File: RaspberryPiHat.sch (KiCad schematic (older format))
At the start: 7 parts, among them J1 Raspberry_Pi_2_3, SW1 SW_DPST, U1 DHT22

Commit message: Finished Schematic
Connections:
- net at J1.1 (3V3): now also R2.2, SW1.1, SW1.3, U1.1 (VCC)
- net at J1.11 (GPIO17): now also R2.1, U1.2 (IO)
- net at J1.6 (GND): now also R1.2, U1.4 (GND)
- net at J1.7 (GCLK0/GPIO4): now also R3.1
- net at J1.8 (GPIO14/TXD): now also R1.1, SW1.2, SW1.4
- net at J1.9 (GND): now also D1.1 (K)
- net at R3.2: now also D1.2 (A)
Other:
- moved on the sheet: D1, R1, R2, R3, SW1, U1
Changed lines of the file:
@@
 L Switch:SW_DPST SW1
 U 1 1 5CDA4549
-P 3200 3025
-F 0 "SW1" H 3200 3350 50  0000 C CNN
-F 1 "SW_DPST" H 3200 3259 50  0000 C CNN
-F 2 "freetronics_footprints:SW_PUSHBUTTON_PTH" H 3200 3025 50  0001 C CNN
-F 3 "~" H 3200 3025 50  0001 C CNN
-	1    3200 3025
+P 3475 2950
+F 0 "SW1" H 3475 3275 50  0000 C CNN
+F 1 "SW_DPST" H 3475 3184 50  0000 C CNN
+F 2 "freetronics_footprints:SW_PUSHBUTTON_PTH" H 3475 2950 50  0001 C CNN
+F 3 "~" H 3475 2950 50  0001 C CNN
+	1    3475 2950
 	1    0    0    -1
 $EndComp
@@
 L Device:R R3
 U 1 1 5CDA6C22
-P 6875 3650
-F 0 "R3" H 6945 3696 50  0000 L CNN
-F 1 "R" H 6945 3605 50  0000 L CNN
-F 2 "Resistor_SMD:R_0805_2012Metric" V 6805 3650 50  0001 C CNN
-F 3 "~" H 6875 3650 50  0001 C CNN
-	1    6875 3650
+P 7150 3725
+F 0 "R3" H 7220 3771 50  0000 L CNN
+F 1 "R" H 7220 3680 50  0000 L CNN
+F 2 "Resistor_SMD:R_0805_2012Metric" V 7080 3725 50  0001 C CNN
+F 3 "~" H 7150 3725 50  0001 C CNN
+	1    7150 3725
 	1    0    0    -1
 $EndComp
@@
 L Device:R R2
 U 1 1 5CDA7C16
-P 4175 2750
-F 0 "R2" H 4245 2796 50  0000 L CNN
-F 1 "R" H 4245 2705 50  0000 L CNN
-F 2 "Resistor_SMD:R_0805_2012Metric" V 4105 2750 50  0001 C CNN
-F 3 "~" H 4175 2750 50  0001 C CNN
-	1    4175 2750
-	1    0    0    -1
+P 4400 3350
+F 0 "R2" V 4193 3350 50  0000 C CNN
+F 1 "R" V 4284 3350 50  0000 C CNN
+F 2 "Resistor_SMD:R_0805_2012Metric" V 4330 3350 50  0001 C CNN
+F 3 "~" H 4400 3350 50  0001 C CNN
+	1    4400 3350
+	0    1    1    0
 $EndComp
 $Comp
 L Device:R R1
 U 1 1 5CDA8690
-P 3225 3800
-F 0 "R1" H 3295 3846 50  0000 L CNN
-F 1 "R" H 3295 3755 50  0000 L CNN
-F 2 "Resistor_SMD:R_0805_2012Metric" V 3155 3800 50  0001 C CNN
-F 3 "~" H 3225 3800 50  0001 C CNN
-	1    3225 3800
+P 3825 3275
+F 0 "R1" H 3895 3321 50  0000 L CNN
+F 1 "R" H 3895 3230 50  0000 L CNN
+F 2 "Resistor_SMD:R_0805_2012Metric" V 3755 3275 50  0001 C CNN
+F 3 "~" H 3825 3275 50  0001 C CNN
+	1    3825 3275
 	1    0    0    -1
 $EndComp
@@
 L Device:LED D1
 U 1 1 5CDA93D6
-P 6875 4100
-F 0 "D1" V 6914 3983 50  0000 R CNN
-F 1 "LED" V 6823 3983 50  0000 R CNN
-F 2 "LED_SMD:LED_0805_2012Metric" H 6875 4100 50  0001 C CNN
-F 3 "~" H 6875 4100 50  0001 C CNN
-	1    6875 4100
+P 7150 4125
+F 0 "D1" V 7189 4008 50  0000 R CNN
+F 1 "LED" V 7098 4008 50  0000 R CNN
+F 2 "LED_SMD:LED_0805_2012Metric" H 7150 4125 50  0001 C CNN
+F 3 "~" H 7150 4125 50  0001 C CNN
+	1    7150 4125
 	0    -1   -1   0
 $EndComp
@@
 L Sensor:DHT11 U1
 U 1 1 5CDAA42C
-P 3975 3350
-F 0 "U1" H 3731 3396 50  0000 R CNN
-F 1 "DHT22" H 3731 3305 50  0000 R CNN
-F 2 "Connector_PinHeader_2.54mm:PinHeader_1x03_P2.54mm_Vertical" H 3975 2950 50  0001 C CNN
-F 3 "http://akizukidenshi.com/download/ds/aosong/DHT11.pdf" H 4125 3600 50  0001 C CNN
-	1    3975 3350
+P 4075 4150
+F 0 "U1" H 3831 4196 50  0000 R CNN
+F 1 "DHT22" H 3831 4105 50  0000 R CNN
+F 2 "Connector_PinHeader_2.54mm:PinHeader_1x03_P2.54mm_Vertical" H 4075 3750 50  0001 C CNN
+F 3 "http://akizukidenshi.com/download/ds/aosong/DHT11.pdf" H 4225 4400 50  0001 C CNN
+	1    4075 4150
 	1    0    0    -1
 $EndComp
+Wire Wire Line
+	7150 4275 7150 5300
+Wire Wire Line
+	7150 5300 5400 5300
+Wire Wire Line
+	5400 5300 5400 5150
+Wire Wire Line
+	7150 3875 7150 3975
+Wire Wire Line
+	7150 3575 7150 3550
+Wire Wire Line
+	7150 3550 6500 3550
+Wire Wire Line
+	5800 2550 5800 2075
+Wire Wire Line
+	5800 2075 4075 2075
+Wire Wire Line
+	4075 2075 4075 3350
+Wire Wire Line
+	4375 4150 4725 4150
+Wire Wire Line
+	4725 4150 4725 3350
+Wire Wire Line
+	4725 3350 4900 3350
+Wire Wire Line
+	4550 3350 4725 3350
+Connection ~ 4725 3350
+Wire Wire Line
+	4250 3350 4075 3350
+Connection ~ 4075 3350
+Wire Wire Line
+	4075 3350 4075 3850
+Wire Wire Line
+	4075 4450 4075 5300
+Wire Wire Line
+	4075 5300 5300 5300
+Wire Wire Line
+	5300 5300 5300 5150
+Wire Wire Line
+	4900 2950 3825 2950
+Wire Wire Line
+	3675 2850 3675 2950
+Connection ~ 3675 2950
+Wire Wire Line
+	3675 2950 3675 3050
+Wire Wire Line
+	3825 3125 3825 2950
+Connection ~ 3825 2950
+Wire Wire Line
+	3825 2950 3675 2950
+Wire Wire Line
+	3825 3425 3825 5300
+Wire Wire Line
+	3825 5300 4075 5300
+Connection ~ 4075 5300
+Wire Wire Line
+	3275 2850 3275 2950
+Wire Wire Line
+	3275 2950 2825 2950
+Wire Wire Line
+	2825 2950 2825 2075
+Wire Wire Line
+	2825 2075 4075 2075
+Connection ~ 3275 2950
+Wire Wire Line
+	3275 2950 3275 3050
+Connection ~ 4075 2075
 $EndSCHEMATC

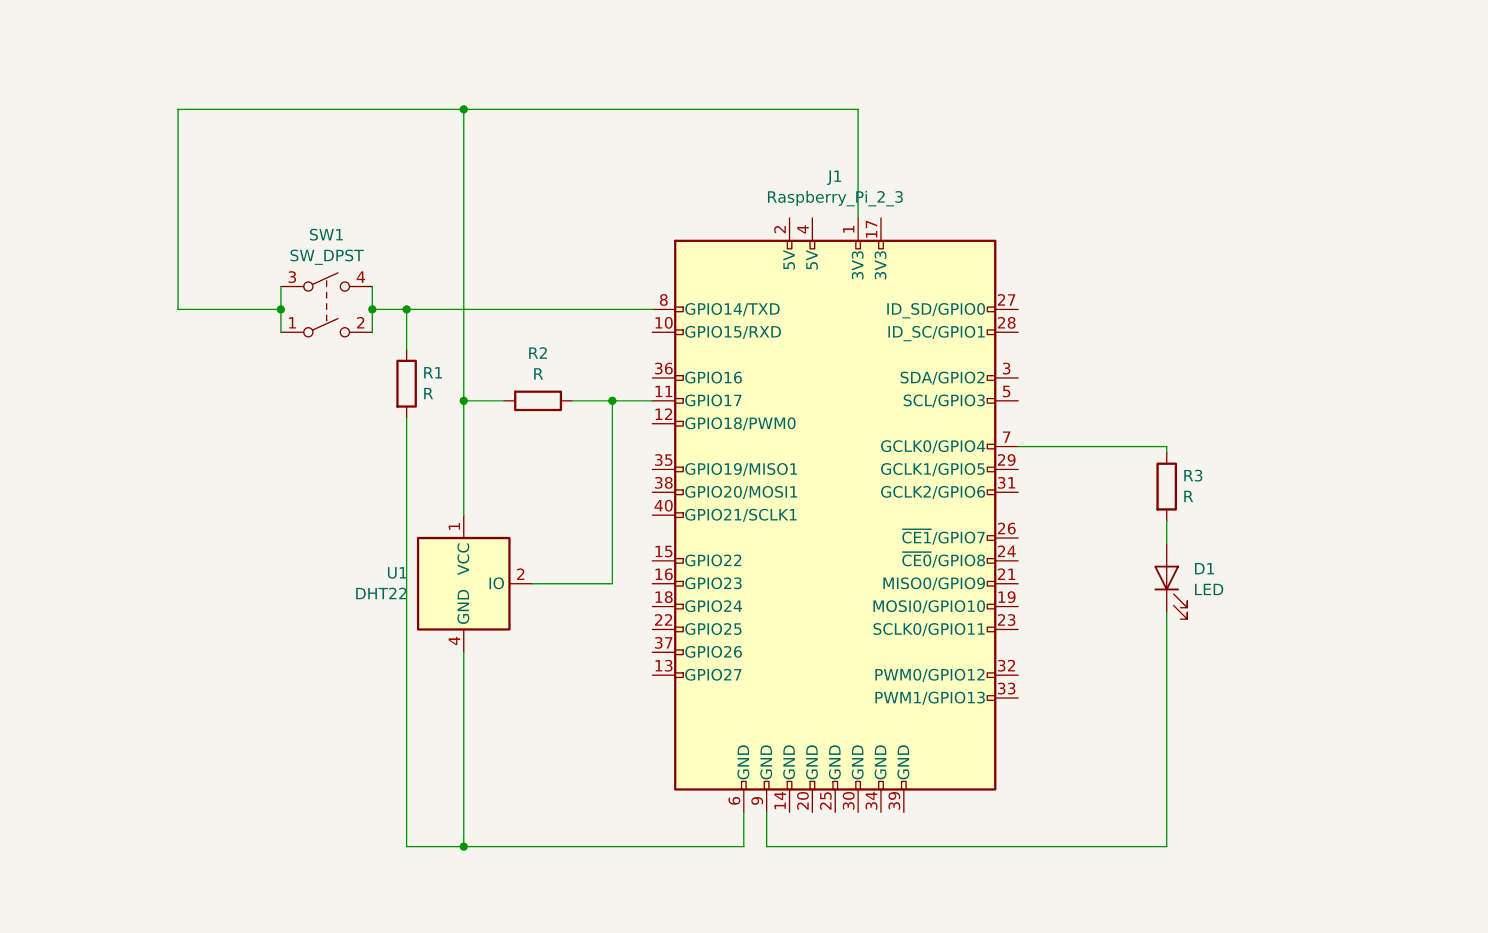
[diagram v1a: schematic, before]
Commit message: Passed DRC
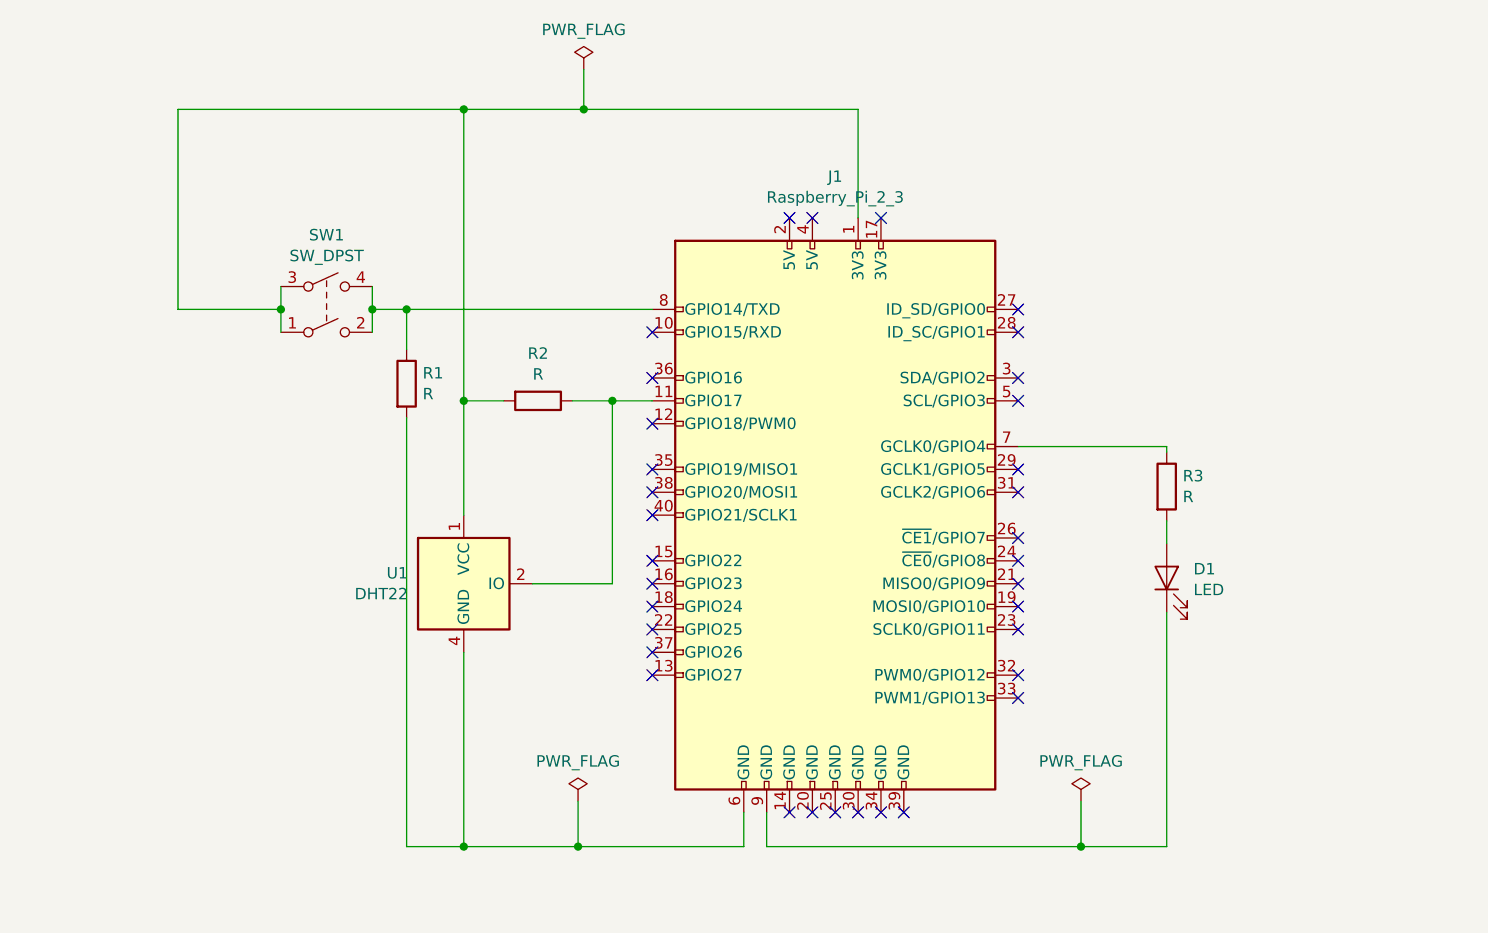
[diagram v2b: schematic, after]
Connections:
- no-connect marks 0 -> 34
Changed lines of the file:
@@
 	7150 4275 7150 5300
 Wire Wire Line
-	7150 5300 5400 5300
+	7150 5300 6775 5300
 Wire Wire Line
 	5400 5300 5400 5150
@@
 	5800 2550 5800 2075
 Wire Wire Line
-	5800 2075 4075 2075
+	5800 2075 4600 2075
 Wire Wire Line
 	4075 2075 4075 3350
@@
 	4075 4450 4075 5300
 Wire Wire Line
-	4075 5300 5300 5300
+	4075 5300 4575 5300
 Wire Wire Line
 	5300 5300 5300 5150
@@
 	3275 2950 3275 3050
 Connection ~ 4075 2075
+NoConn ~ 4900 3050
+NoConn ~ 4900 3250
+NoConn ~ 4900 3450
+NoConn ~ 4900 3650
+NoConn ~ 4900 3750
+NoConn ~ 4900 3850
+NoConn ~ 4900 4050
+NoConn ~ 4900 4150
+NoConn ~ 4900 4250
+NoConn ~ 4900 4350
+NoConn ~ 4900 4450
+NoConn ~ 4900 4550
+NoConn ~ 5500 5150
+NoConn ~ 5600 5150
+NoConn ~ 5700 5150
+NoConn ~ 5800 5150
+NoConn ~ 5900 5150
+NoConn ~ 6000 5150
+NoConn ~ 6500 4650
+NoConn ~ 6500 4550
+NoConn ~ 6500 4350
+NoConn ~ 6500 4250
+NoConn ~ 6500 4150
+NoConn ~ 6500 4050
+NoConn ~ 6500 3950
+NoConn ~ 6500 3750
+NoConn ~ 6500 3650
+NoConn ~ 6500 3350
+NoConn ~ 6500 3250
+NoConn ~ 6500 3050
+NoConn ~ 6500 2950
+NoConn ~ 5900 2550
+NoConn ~ 5600 2550
+NoConn ~ 5500 2550
+$Comp
+L power:PWR_FLAG #FLG0101
+U 1 1 5CDD84E3
+P 4600 1900
+F 0 "#FLG0101" H 4600 1975 50  0001 C CNN
+F 1 "PWR_FLAG" H 4600 2073 50  0000 C CNN
+F 2 "" H 4600 1900 50  0001 C CNN
+F 3 "~" H 4600 1900 50  0001 C CNN
+	1    4600 1900
+	1    0    0    -1
+$EndComp
+Wire Wire Line
+	4600 1900 4600 2075
+Connection ~ 4600 2075
+Wire Wire Line
+	4600 2075 4075 2075
+$Comp
+L power:PWR_FLAG #FLG0102
+U 1 1 5CDD996D
+P 4575 5100
+F 0 "#FLG0102" H 4575 5175 50  0001 C CNN
+F 1 "PWR_FLAG" H 4575 5273 50  0000 C CNN
+F 2 "" H 4575 5100 50  0001 C CNN
+F 3 "~" H 4575 5100 50  0001 C CNN
+	1    4575 5100
+	1    0    0    -1
+$EndComp
+$Comp
+L power:PWR_FLAG #FLG0103
+U 1 1 5CDDA483
+P 6775 5100
+F 0 "#FLG0103" H 6775 5175 50  0001 C CNN
+F 1 "PWR_FLAG" H 6775 5273 50  0000 C CNN
+F 2 "" H 6775 5100 50  0001 C CNN
+F 3 "~" H 6775 5100 50  0001 C CNN
+	1    6775 5100
+	1    0    0    -1
+$EndComp
+Wire Wire Line
+	4575 5100 4575 5300
+Connection ~ 4575 5300
+Wire Wire Line
+	4575 5300 5300 5300
+Wire Wire Line
+	6775 5100 6775 5300
+Connection ~ 6775 5300
+Wire Wire Line
+	6775 5300 5400 5300
 $EndSCHEMATC

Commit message: generated netlist
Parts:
- added D2: LED, LED_SMD:LED_0805_2012Metric, symbol Device:LED
- added R4: R, Resistor_SMD:R_0805_2012Metric, symbol Device:R
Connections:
- net 3v3: now reaches J1.1 (3V3), R2.2, SW1.1, SW1.3, U1.1 (VCC)
- net 3v3: now also R4.1
- net GND: now reaches J1.6 (GND), R1.2, U1.4 (GND)
- net GND: now also D1.1 (K), J1.9 (GND), D2.1 (K)
- net button_input: now reaches J1.8 (GPIO14/TXD), R1.1, SW1.2, SW1.4
- new net: D2.2 (A), R4.2
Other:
- note added: "N1 - Momentary Button\n"
- note added: "N2 - Sensor"
- note added: "N3 - Raspberry Pi"
- note added: "N4 - Inidcator LED"
- note added: "N5 - Power LED"
- moved on the sheet: R1, SW1

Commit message: Updated files
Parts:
- J1: footprint Connector_PinSocket_2.54mm:PinSocket_2x08_P2.54mm_Vertical -> Connector_PinHeader_2.54mm:PinHeader_2x08_P2.54mm_Vertical
- U1: footprint Connector_PinHeader_2.54mm:PinHeader_1x03_P2.54mm_Vertical -> Connector_PinHeader_2.54mm:PinHeader_1x04_P2.54mm_Vertical
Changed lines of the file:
@@
 F 0 "J1" H 6025 5350 50  0000 C CNN
 F 1 "Raspberry_Pi_2_3" H 6300 5250 50  0000 C CNN
-F 2 "Connector_PinSocket_2.54mm:PinSocket_2x08_P2.54mm_Vertical" H 5700 3850 50  0001 C CNN
+F 2 "Connector_PinHeader_2.54mm:PinHeader_2x08_P2.54mm_Vertical" H 5700 3850 50  0001 C CNN
 F 3 "https://www.raspberrypi.org/documentation/hardware/raspberrypi/schematics/rpi_SCH_3bplus_1p0_reduced.pdf" H 5700 3850 50  0001 C CNN
 	1    5700 3850
@@
 	1    7150 4125
 	0    -1   -1   0
-$EndComp
-$Comp
-L Sensor:DHT11 U1
-U 1 1 5CDAA42C
-P 4075 4150
-F 0 "U1" H 3831 4196 50  0000 R CNN
-F 1 "DHT22" H 3831 4105 50  0000 R CNN
-F 2 "Connector_PinHeader_2.54mm:PinHeader_1x03_P2.54mm_Vertical" H 4075 3750 50  0001 C CNN
-F 3 "http://akizukidenshi.com/download/ds/aosong/DHT11.pdf" H 4225 4400 50  0001 C CNN
-	1    4075 4150
-	1    0    0    -1
 $EndComp
 Wire Wire Line
@@
 Text Notes 7650 2225 0    50   ~ 0
 N5 - Power LED
+$Comp
+L Sensor:DHT11 U1
+U 1 1 5CDAA42C
+P 4075 4150
+F 0 "U1" H 3831 4196 50  0000 R CNN
+F 1 "DHT22" H 3831 4105 50  0000 R CNN
+F 2 "Connector_PinHeader_2.54mm:PinHeader_1x04_P2.54mm_Vertical" H 4075 3750 50  0001 C CNN
+F 3 "http://akizukidenshi.com/download/ds/aosong/DHT11.pdf" H 4225 4400 50  0001 C CNN
+	1    4075 4150
+	1    0    0    -1
+$EndComp
 $EndSCHEMATC
